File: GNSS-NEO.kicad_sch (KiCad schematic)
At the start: 72 parts, among them J3 Conn_Coaxial, J4 Conn_Coaxial_Small, Q2 AO3401A, Q5 BSS138, SW1 SW_Push, SW2 SW_Push, U2 NEO-M9N, U8 TPS259474LRPWR

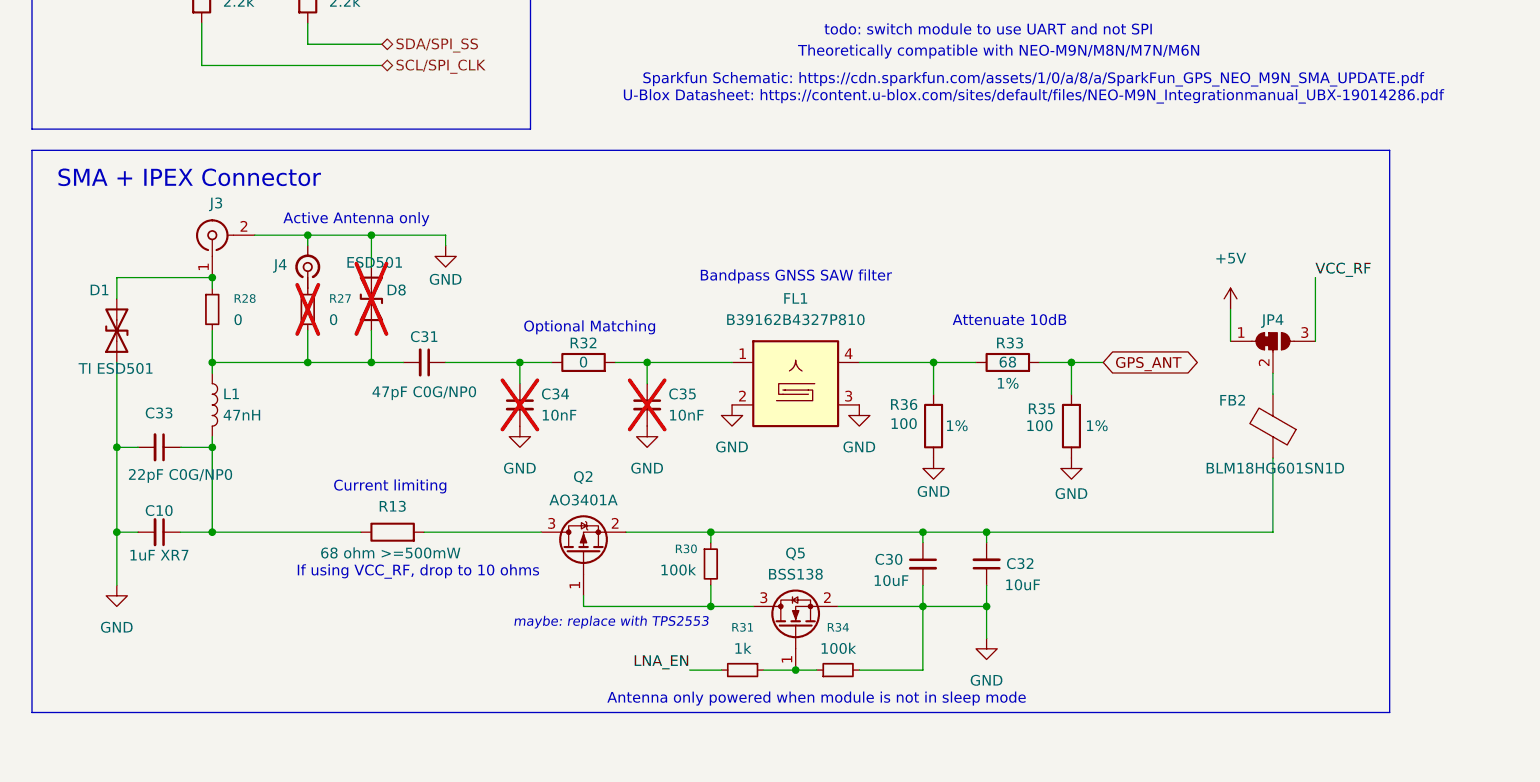
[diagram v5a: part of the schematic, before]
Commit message: wired BQ25798 schematic
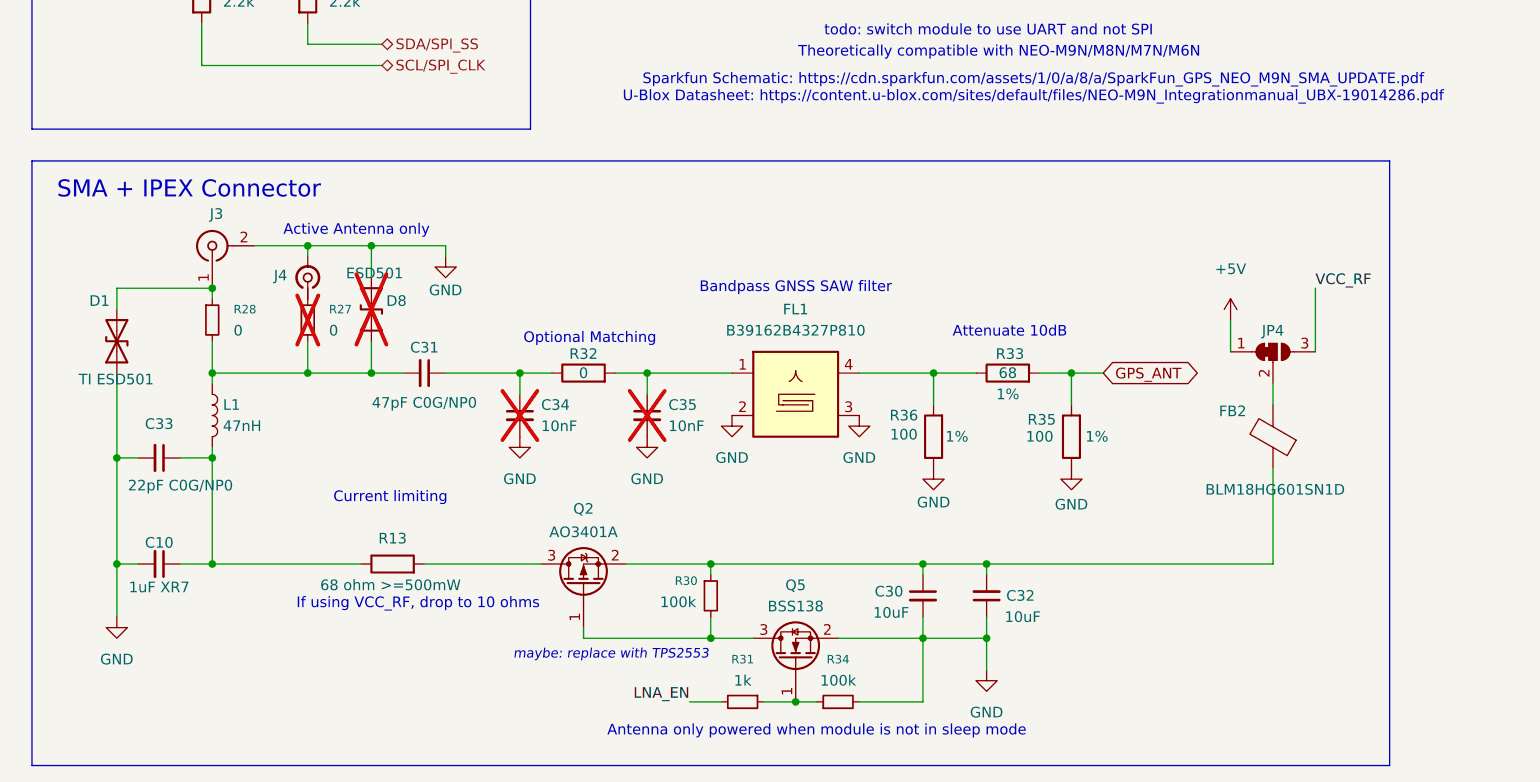
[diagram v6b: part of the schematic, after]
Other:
- moved on the sheet: C10, C30, C31, C32, C33, C34, C35, D1, D8, FB2, FL1, J3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
